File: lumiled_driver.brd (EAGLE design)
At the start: 51 x 38 mm, 20 parts, among them X1 PWR

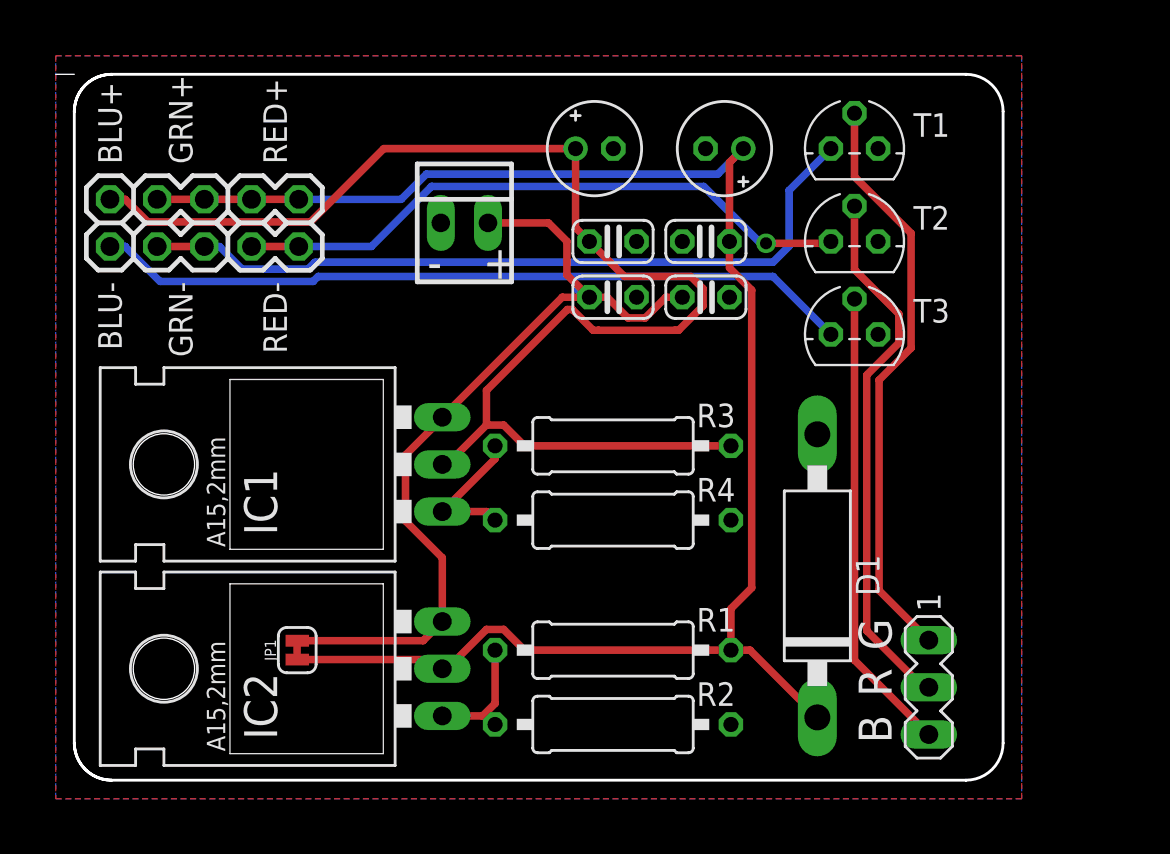
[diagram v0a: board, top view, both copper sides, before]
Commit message: -changed design to use MOSFETs
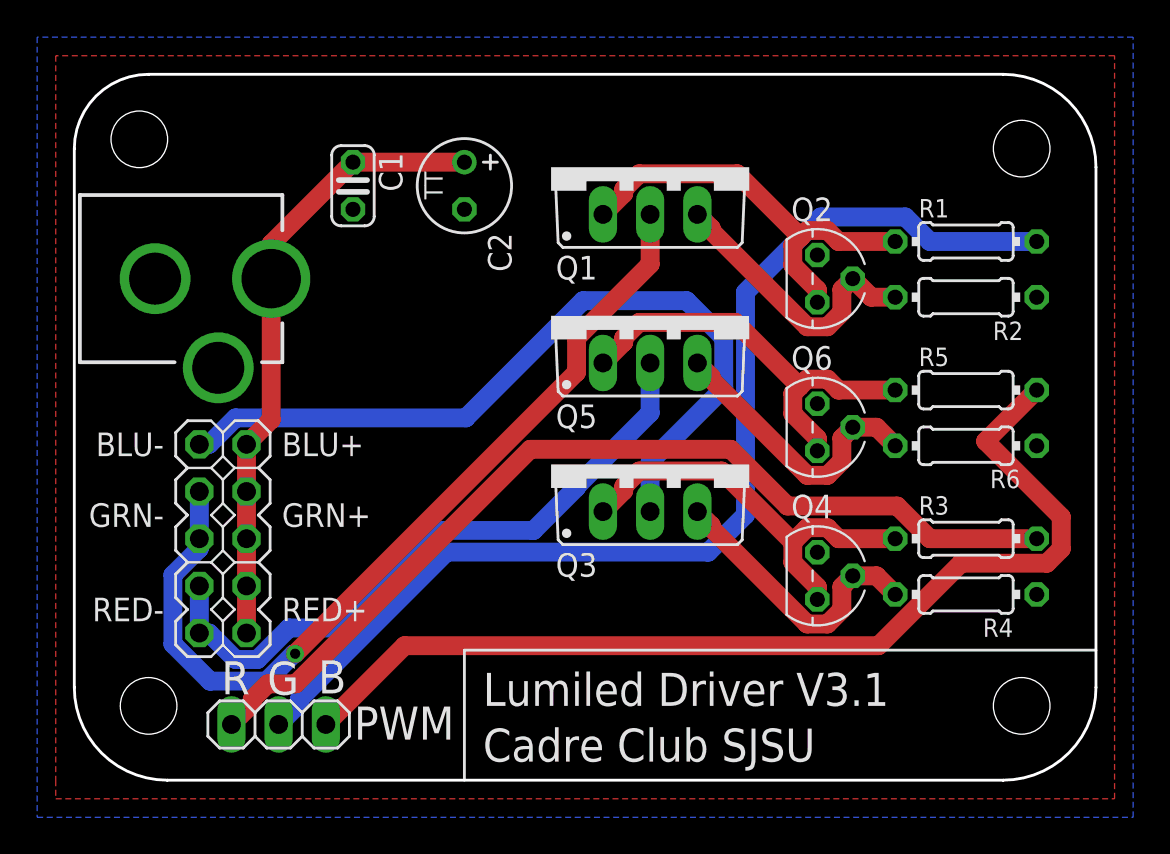
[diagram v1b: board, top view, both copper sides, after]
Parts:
- removed C3, C5, C6: 100nF, rcl:C025-024X044
- removed C4: 10uF, rcl:E2-5
- removed D1: (no value), diode:C1702-15
- removed IC1, IC2: (no value), v-reg:317TL
- removed SV1: (no value), con-lstb:MA03-1
- removed T1, T2, T3: (no value), transistor:TO92
- removed X1: PWR, con-molex:22-23-2021
- added CN1: (no value), adafruit:DCJACK_2MM_PTH
- added Q1, Q3, Q5: IRF520, transistor-power:TO220BV
- added Q2, Q4, Q6: 2N3904, transistor-npn:TO92
- added R5, R6: (no value), rcl:0204/7
- C1: value 10uF -> 100nF; device rcl:E2-5 -> rcl:C025-024X044
- C2: device rcl:C025-024X044 -> resistor:TT2D5
- JP1: value 12V BYPASS -> (none); device SparkFun-Jumpers:SMT-JUMPER_2_NC_TRACE_SILK -> pinhead:1X03
- R1, R2, R3, R4: device resistor:0309/12 -> rcl:0204/7
- moved R2 29.8 mm to (48.0, 26.0)
- moved R1 29.1 mm to (48.0, 29.0)
- moved R3 19.6 mm to (48.0, 13.0)
- moved R4 19.4 mm to (48.0, 10.0)
- moved U$1 17.0 mm to (8.00, 13.0), turned to 90 degrees
- moved C1 13.2 mm to (15.0, 32.0), turned to 270 degrees
- moved C2 10.0 mm to (21.0, 32.0), turned to 270 degrees
- moved JP1 4.12 mm to (11.0, 3.00), turned to 180 degrees
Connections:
- removed net N$1: T1.3, U$1.6, U$1.8
- removed net N$2: T2.3, U$1.2, U$1.4
- removed net N$3: T3.3, U$1.10
- removed net N$4: C1.+, C5.1, IC1.2, R3.2, U$1.9
- removed net N$6: C4.+, C6.1, D1.C, IC2.2, JP1.1, R1.2, U$1.1, U$1.3, U$1.5, U$1.7
- removed net N$7: IC2.1, R1.1, R2.2
- removed net N$8: IC1.1, R3.1, R4.2
- new net N$10: Q1.D, U$1.6, U$1.8
- new net N$17: Q1.G, Q2.1, R1.1
- new net N$18: Q3.G, Q4.1, R3.1
- new net N$19: Q5.G, Q6.1, R5.1
- new net N$20: Q1.S, Q2.2, R2.2
- new net N$21: Q3.S, Q4.2, R4.2
- new net N$22: Q5.S, Q6.2, R6.2
- new net N$26: Q3.D, U$1.10
- new net N$27: Q5.D, U$1.2, U$1.4
- net +VIN: now also C1.1, C2.+, CN1.PWR, U$1.1, U$1.3, U$1.5, U$1.7, U$1.9; no longer C2.1, C3.1, IC1.3, IC2.3, JP1.2, X1.2
- net BLU_PWM: now also JP1.1, R5.2; no longer SV1.3, T3.2
- net GND: now also C1.2, C2.-, CN1.GND, CN1.GNDBREAK, Q2.3, Q4.3, Q6.3, R6.1; no longer C1.-, C2.2, C3.2, C4.-, C5.2, C6.2, D1.A, T1.1, T2.1, T3.1, X1.1
- net GRN_PWM: now also JP1.2, R1.2; no longer SV1.1, T1.2
- net RED_PWM: now also JP1.3, R3.2; no longer SV1.2, T2.2
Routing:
- net N$6: track 92.4 -> 0.00 mm
- net N$4: track 73.8 -> 0.00 mm
- net N$10: track 0.00 -> 48.4 mm, vias 0 -> 1
- net N$26: track 0.00 -> 43.3 mm
- net N$3: track 41.8 -> 0.00 mm
- net N$1: track 41.2 -> 0.00 mm
- net N$27: track 0.00 -> 35.6 mm
- net N$2: track 33.8 -> 0.00 mm, vias 1 -> 0
- net BLU_PWM: track 25.1 -> 54.9 mm
- net GRN_PWM: track 31.5 -> 59.8 mm
- net N$17: track 0.00 -> 22.8 mm
- net N$19: track 0.00 -> 22.8 mm
- net N$18: track 0.00 -> 22.6 mm
- net RED_PWM: track 29.2 -> 51.6 mm
- net N$22: track 0.00 -> 15.4 mm
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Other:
- board size 51 x 38 mm -> 55 x 38 mm
- board text added: "Cadre Club SJSU"
- board text added: "Lumiled Driver V3.1"
- board text added: "PWM"
- board text removed: "+"
- board text removed: "-"
- board text removed: "Lumiled Board V1.0"
